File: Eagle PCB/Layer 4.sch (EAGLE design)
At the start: 49 parts, among them X1 SM06B-SRSS-TB, Y1 8MHz

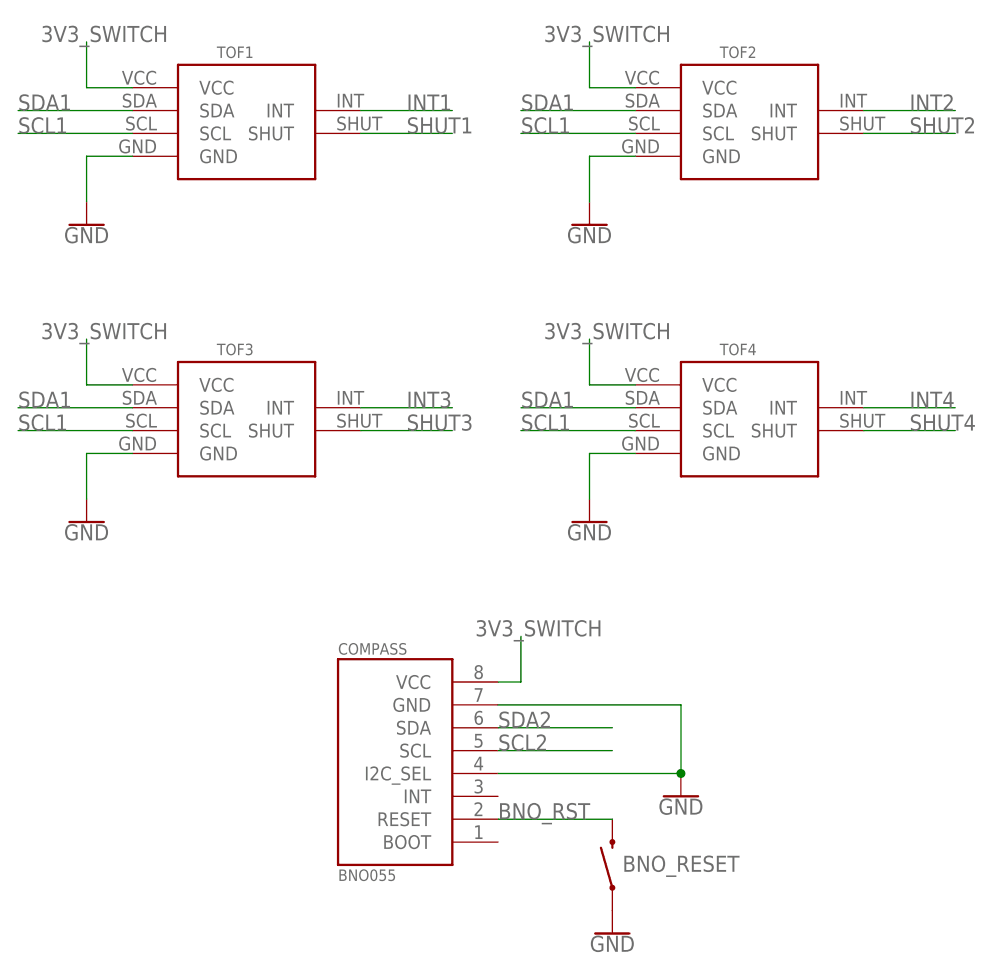
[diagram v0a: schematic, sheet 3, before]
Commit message: layer 1 esc fix
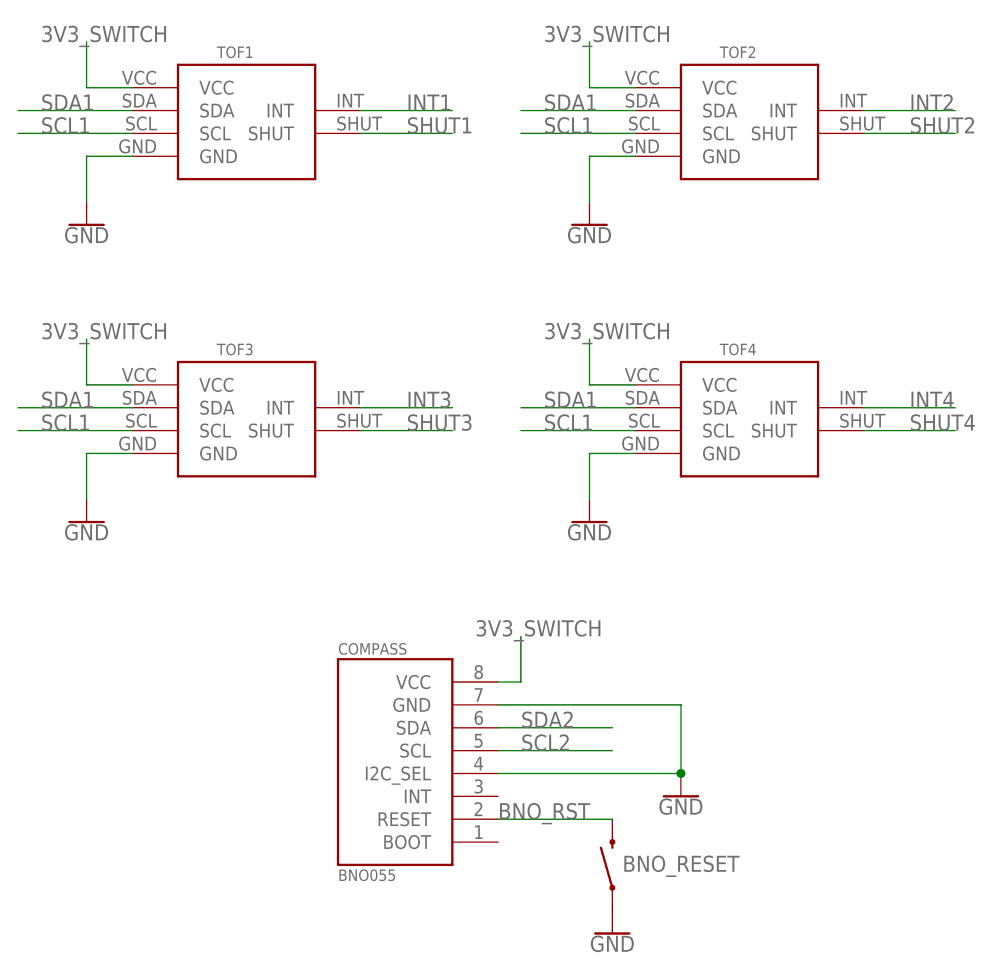
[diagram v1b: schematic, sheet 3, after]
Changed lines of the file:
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@@
-</segment>
-</net>
-<net name="SDA1" class="0">
-<segment>
-<wire x1="50.8" y1="149.86" x2="38.1" y2="149.86" width="0.1524" layer="91"/>
-<label x="38.1" y="149.86" size="1.778" layer="95"/>
-<pinref part="TOF1" gate="G$1" pin="SDA"/>
-</segment>
-<segment>
-<wire x1="106.68" y1="149.86" x2="93.98" y2="149.86" width="0.1524" layer="91"/>
-<label x="93.98" y="149.86" size="1.778" layer="95"/>
-<pinref part="TOF2" gate="G$1" pin="SDA"/>
-</segment>
-<segment>
-<wire x1="50.8" y1="116.84" x2="38.1" y2="116.84" width="0.1524" layer="91"/>
-<label x="38.1" y="116.84" size="1.778" layer="95"/>
-<pinref part="TOF3" gate="G$1" pin="SDA"/>
-</segment>
-<segment>
-<wire x1="106.68" y1="116.84" x2="93.98" y2="116.84" width="0.1524" layer="91"/>
-<label x="93.98" y="116.84" size="1.778" layer="95"/>
-<pinref part="TOF4" gate="G$1" pin="SDA"/>
-</segment>
-</net>
-<net name="SCL1" class="0">
-<segment>
-<wire x1="50.8" y1="147.32" x2="38.1" y2="147.32" width="0.1524" layer="91"/>
-<label x="38.1" y="147.32" size="1.778" layer="95"/>
-<pinref part="TOF1" gate="G$1" pin="SCL"/>
-</segment>
-<segment>
-<wire x1="106.68" y1="147.32" x2="93.98" y2="147.32" width="0.1524" layer="91"/>
-<label x="93.98" y="147.32" size="1.778" layer="95"/>
-<pinref part="TOF2" gate="G$1" pin="SCL"/>
-</segment>
-<segment>
-<wire x1="50.8" y1="114.3" x2="38.1" y2="114.3" width="0.1524" layer="91"/>
-<label x="38.1" y="114.3" size="1.778" layer="95"/>
-<pinref part="TOF3" gate="G$1" pin="SCL"/>
-</segment>
-<segment>
-<wire x1="106.68" y1="114.3" x2="93.98" y2="114.3" width="0.1524" layer="91"/>
-<label x="93.98" y="114.3" size="1.778" layer="95"/>
-<pinref part="TOF4" gate="G$1" pin="SCL"/>
 </segment>
 </net>
@@
 </segment>
 </net>
-<net name="SDA2" class="0">
-<segment>
-<pinref part="COMPASS" gate="G$1" pin="SDA"/>
-<wire x1="91.44" y1="81.28" x2="104.14" y2="81.28" width="0.1524" layer="91"/>
-<label x="91.44" y="81.28" size="1.778" layer="95"/>
-</segment>
-</net>
-<net name="SCL2" class="0">
-<segment>
-<pinref part="COMPASS" gate="G$1" pin="SCL"/>
-<wire x1="91.44" y1="78.74" x2="104.14" y2="78.74" width="0.1524" layer="91"/>
-<label x="91.44" y="78.74" size="1.778" layer="95"/>
-</segment>
-</net>
 <net name="3V3_SWITCH" class="0">
 <segment>
@@
 </segment>
 </net>
+<net name="SDA1" class="0">
+<segment>
+<pinref part="TOF1" gate="G$1" pin="SDA"/>
+<wire x1="50.8" y1="149.86" x2="38.1" y2="149.86" width="0.1524" layer="91"/>
+<label x="40.64" y="149.86" size="1.778" layer="95"/>
+</segment>
+<segment>
+<wire x1="106.68" y1="149.86" x2="93.98" y2="149.86" width="0.1524" layer="91"/>
+<pinref part="TOF2" gate="G$1" pin="SDA"/>
+<label x="96.52" y="149.86" size="1.778" layer="95"/>
+</segment>
+<segment>
+<pinref part="TOF3" gate="G$1" pin="SDA"/>
+<wire x1="50.8" y1="116.84" x2="38.1" y2="116.84" width="0.1524" layer="91"/>
+<label x="40.64" y="116.84" size="1.778" layer="95"/>
+</segment>
+<segment>
+<pinref part="TOF4" gate="G$1" pin="SDA"/>
+<wire x1="106.68" y1="116.84" x2="93.98" y2="116.84" width="0.1524" layer="91"/>
+<label x="96.52" y="116.84" size="1.778" layer="95"/>
+</segment>
+</net>
+<net name="SCL1" class="0">
+<segment>
+<pinref part="TOF1" gate="G$1" pin="SCL"/>
+<wire x1="50.8" y1="147.32" x2="38.1" y2="147.32" width="0.1524" layer="91"/>
+<label x="40.64" y="147.32" size="1.778" layer="95"/>
+</segment>
+<segment>
+<wire x1="106.68" y1="147.32" x2="93.98" y2="147.32" width="0.1524" layer="91"/>
+<pinref part="TOF2" gate="G$1" pin="SCL"/>
+<label x="96.52" y="147.32" size="1.778" layer="95"/>
+</segment>
+<segment>
+<pinref part="TOF3" gate="G$1" pin="SCL"/>
+<wire x1="50.8" y1="114.3" x2="38.1" y2="114.3" width="0.1524" layer="91"/>
+<label x="40.64" y="114.3" size="1.778" layer="95"/>
+</segment>
+<segment>
+<pinref part="TOF4" gate="G$1" pin="SCL"/>
+<wire x1="106.68" y1="114.3" x2="93.98" y2="114.3" width="0.1524" layer="91"/>
+<label x="96.52" y="114.3" size="1.778" layer="95"/>
+</segment>
+</net>
+<net name="SDA2" class="0">
+<segment>
+<pinref part="COMPASS" gate="G$1" pin="SDA"/>
+<wire x1="91.44" y1="81.28" x2="104.14" y2="81.28" width="0.1524" layer="91"/>
+<label x="93.98" y="81.28" size="1.778" layer="95"/>
+</segment>
+</net>
+<net name="SCL2" class="0">
+<segment>
+<pinref part="COMPASS" gate="G$1" pin="SCL"/>
+<wire x1="91.44" y1="78.74" x2="104.14" y2="78.74" width="0.1524" layer="91"/>
+<label x="93.98" y="78.74" size="1.778" layer="95"/>
+</segment>
+</net>
